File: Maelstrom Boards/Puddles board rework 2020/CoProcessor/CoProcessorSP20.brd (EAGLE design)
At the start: 101.6 x 101.6 mm, 77 parts, among them J1 USB_MINI-B_SMT, P1 RB1-125BAG1A, Q1 310mA/60V/1.6Ω, Q2 310mA/60V/1.6Ω, Q3 310mA/60V/1.6Ω, Q4 310mA/60V/1.6Ω, Q5 310mA/60V/1.6Ω, Q6 310mA/60V/1.6Ω, Q7 310mA/60V/1.6Ω, Q8 310mA/60V/1.6Ω, U1 W5500, U2 STM32F405RGT6, Y1 12MHz, Y2 25MHz, Y3 32.768kHz

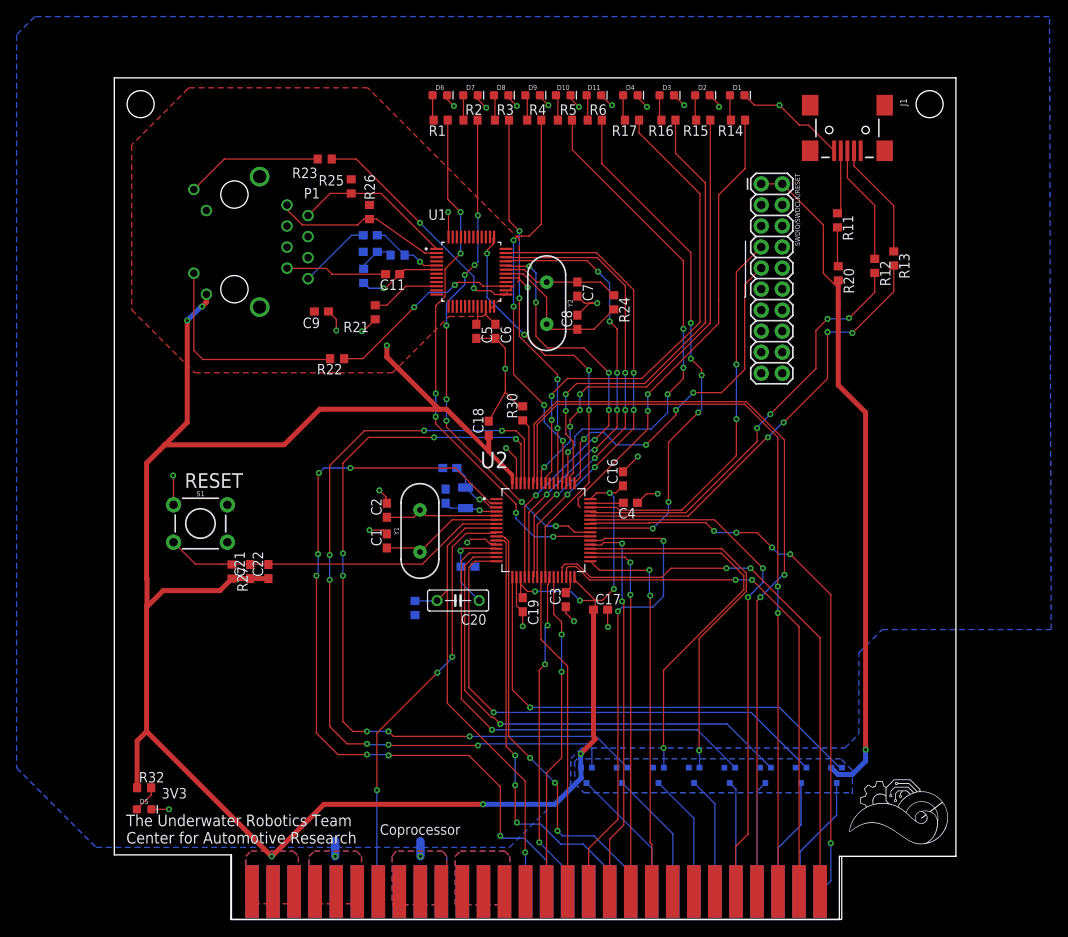
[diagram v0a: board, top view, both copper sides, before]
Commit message: updated puddles board rework ESC and Copro finished
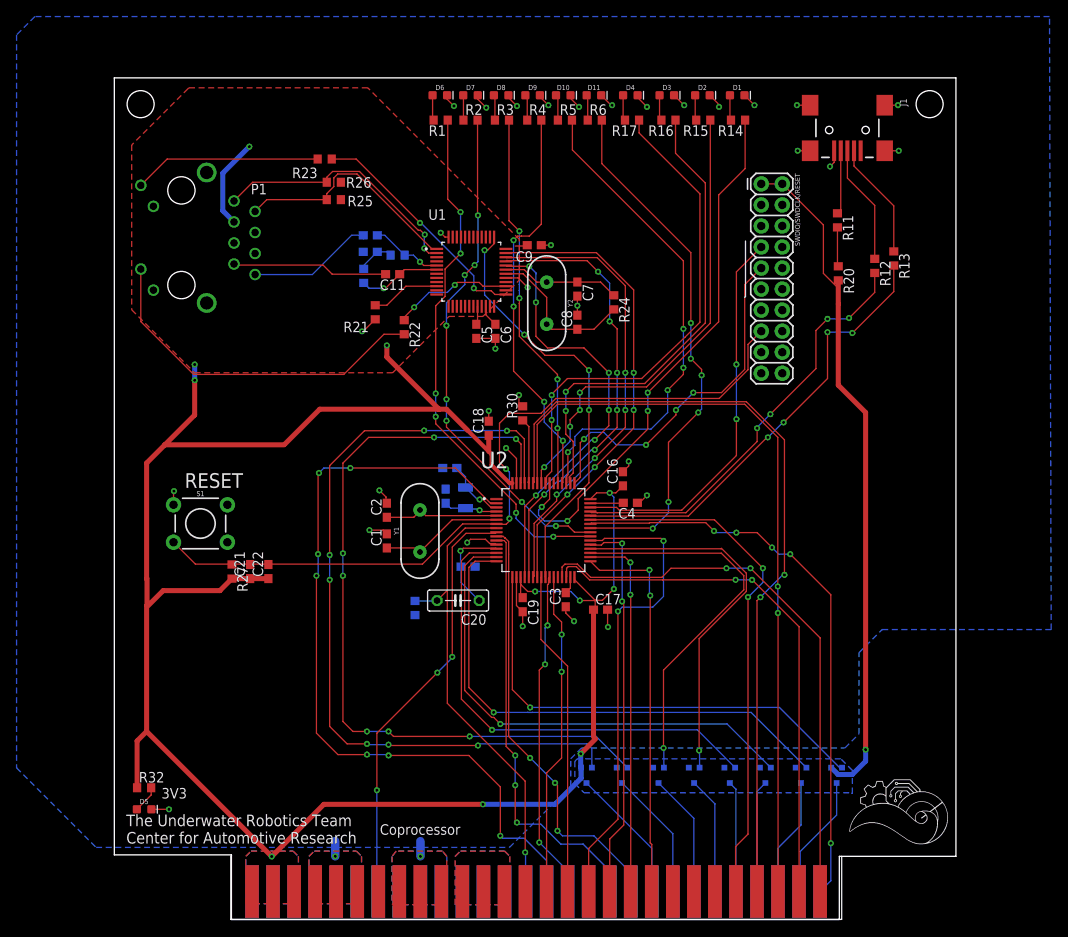
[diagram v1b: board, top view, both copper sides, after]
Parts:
- R1: value 5 -> 65
- R4, R5: value 65 -> 5
- moved C9 26.9 mm to (50.7, 81.4)
- moved R22 8.95 mm to (35.0, 71.5), turned to 270 degrees
- moved P1 6.42 mm to (8.10, 82.3)
- moved R26 5.61 mm to (26.5, 89.0), turned to 0 degrees
- moved R25 2.64 mm to (26.5, 86.9), turned to 0 degrees
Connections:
- removed net N$34: C21.2, C22.2, R27.1, S1.3, U2.7
- new net RESET: C21.2, C22.2, R27.1, S1.3, SWDIO/SWDCLK/RESET.15, U2.7
- net GND: now also J1.S1, J1.S2, J1.S3, J1.S4
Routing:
- net RESET: track 0.00 -> 94.6 mm, vias 0 -> 2
- net N$34: track 42.2 -> 0.00 mm
- net GND: track 103.0 -> 78.8 mm, vias 29 -> 36
- net N$20: track 26.3 -> 42.8 mm
- net N$17: track 21.0 -> 31.6 mm, vias 0 -> 2
- net LED_RED: track 55.2 -> 65.5 mm, vias 2 -> 4
- net N$16: track 19.4 -> 28.6 mm
- net N$22: track 23.5 -> 14.6 mm
- net N$27: track 12.2 -> 18.8 mm
- net N$21: track 16.5 -> 22.7 mm
- net N$26: track 9.28 -> 15.5 mm
- net +3V3: track 357.6 -> 361.0 mm, vias 12 -> 13

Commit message: final commit for ESC board, resistor values changed across boards for order ease
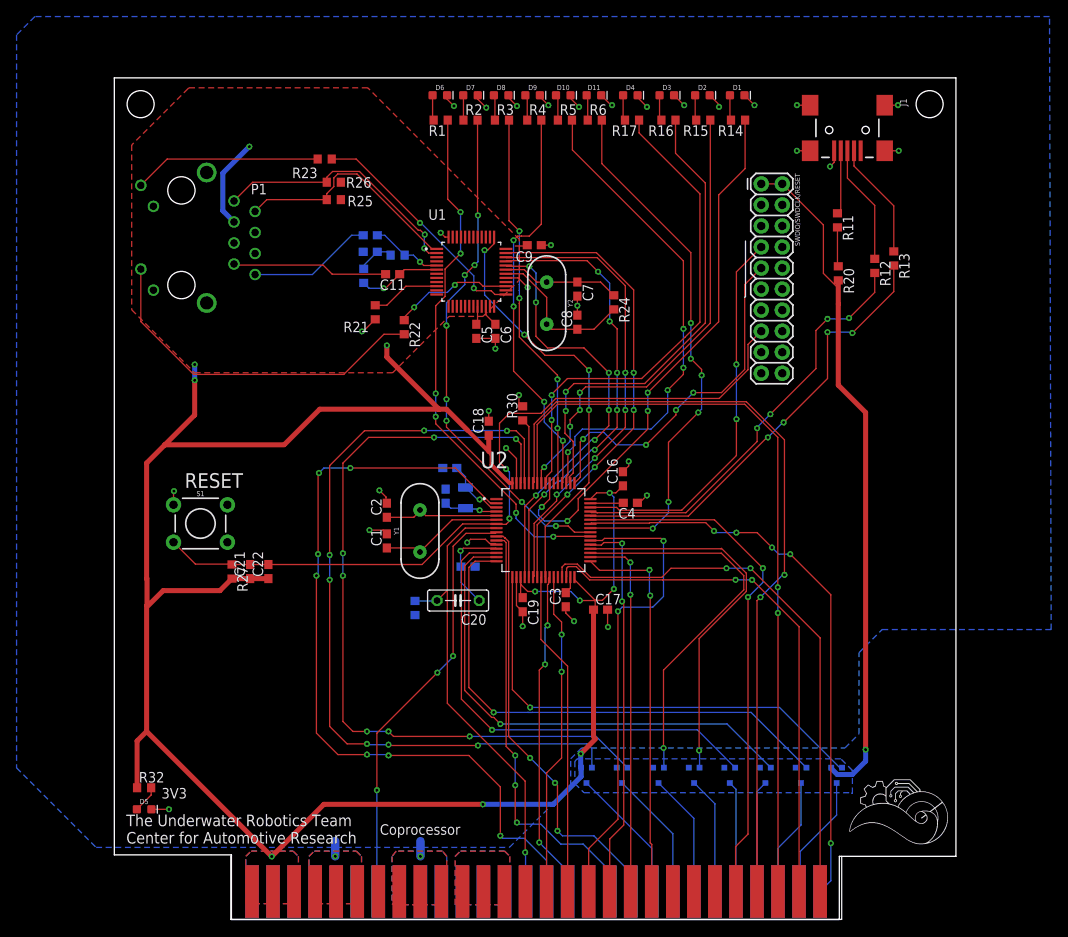
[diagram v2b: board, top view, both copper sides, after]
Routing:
- net PWM_CH1: track 19.2 -> 16.4 mm
- net 5V_CNTRL: track 97.5 -> 96.3 mm
- net MOBO_CNTRL: track 53.0 -> 52.5 mm

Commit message: Changing puddles values
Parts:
- C1, C2, C7, C8: value 18pF -> 30pF
- C13, C14: value 12.5pF -> 18pF
- R1, R14, R15, R2, R3, R6: value 65 -> 68
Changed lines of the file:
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@@
 <?xml version="1.0" encoding="utf-8"?>
 <!DOCTYPE eagle SYSTEM "eagle.dtd">
-<eagle version="9.5.2">
+<eagle version="9.6.2">
 <drawing>
 <settings>
@@
 <attribute name="VALUE" x="62.3" y="98.865" size="0.6096" layer="27" font="vector" ratio="20" align="top-center"/>
 </element>
-<element name="R14" library="rcl" library_urn="urn:adsk.eagle:library:334" package="R0603" package3d_urn="urn:adsk.eagle:package:23555/2" value="65" x="75.3" y="96.5" smashed="yes" rot="R180">
+<element name="R14" library="rcl" library_urn="urn:adsk.eagle:library:334" package="R0603" package3d_urn="urn:adsk.eagle:package:23555/2" value="68" x="75.3" y="96.5" smashed="yes" rot="R180">
 <attribute name="NAME" x="75.935" y="95.865" size="1.27" layer="25" rot="R180"/>
 <attribute name="SPICEPREFIX" value="R" x="94.9" y="154.3" size="1.778" layer="27" rot="R180" display="off"/>
 <attribute name="VALUE" x="75.935" y="98.405" size="1.27" layer="27" rot="R180"/>
 </element>
-<element name="R15" library="rcl" library_urn="urn:adsk.eagle:library:334" package="R0603" package3d_urn="urn:adsk.eagle:package:23555/2" value="65" x="71.1" y="96.5" smashed="yes" rot="R180">
+<element name="R15" library="rcl" library_urn="urn:adsk.eagle:library:334" package="R0603" package3d_urn="urn:adsk.eagle:package:23555/2" value="68" x="71.1" y="96.5" smashed="yes" rot="R180">
 <attribute name="NAME" x="71.735" y="95.865" size="1.27" layer="25" rot="R180"/>
 <attribute name="SPICEPREFIX" value="R" x="95.4" y="157.8" size="1.778" layer="27" rot="R180" display="off"/>
@@
 <attribute name="VALUE" x="39.44" y="46.9" size="0.6096" layer="27" font="vector" ratio="20" rot="R90" align="top-center"/>
 </element>
-<element name="C1" library="rcl" library_urn="urn:adsk.eagle:library:334" package="C0603" package3d_urn="urn:adsk.eagle:package:23616/2" value="18pF" x="32.9" y="45.7" smashed="yes" rot="R90">
+<element name="C1" library="rcl" library_urn="urn:adsk.eagle:library:334" package="C0603" package3d_urn="urn:adsk.eagle:package:23616/2" value="30pF" x="32.9" y="45.7" smashed="yes" rot="R90">
 <attribute name="NAME" x="32.265" y="45.065" size="1.27" layer="25" rot="R90"/>
 <attribute name="SPICEPREFIX" value="C" x="121.4" y="7.3" size="1.778" layer="27" rot="R90" display="off"/>
 <attribute name="VALUE" x="34.805" y="45.065" size="1.27" layer="27" rot="R90"/>
 </element>
-<element name="C2" library="rcl" library_urn="urn:adsk.eagle:library:334" package="C0603" package3d_urn="urn:adsk.eagle:package:23616/2" value="18pF" x="32.9" y="49.4" smashed="yes" rot="R90">
+<element name="C2" library="rcl" library_urn="urn:adsk.eagle:library:334" package="C0603" package3d_urn="urn:adsk.eagle:package:23616/2" value="30pF" x="32.9" y="49.4" smashed="yes" rot="R90">
 <attribute name="NAME" x="32.265" y="48.765" size="1.27" layer="25" rot="R90"/>
 <attribute name="SPICEPREFIX" value="C" x="124.9" y="7.3" size="1.778" layer="27" rot="R90" display="off"/>
@@
 <attribute name="VALUE" x="49.66" y="74.4" size="0.6096" layer="27" font="vector" ratio="20" rot="R270" align="top-center"/>
 </element>
-<element name="C7" library="rcl" library_urn="urn:adsk.eagle:library:334" package="C0603" package3d_urn="urn:adsk.eagle:package:23616/2" value="18pF" x="55.9" y="76.1" smashed="yes" rot="R270">
+<element name="C7" library="rcl" library_urn="urn:adsk.eagle:library:334" package="C0603" package3d_urn="urn:adsk.eagle:package:23616/2" value="30pF" x="55.9" y="76.1" smashed="yes" rot="R270">
 <attribute name="NAME" x="56.535" y="76.735" size="1.27" layer="25" rot="R270"/>
 <attribute name="SPICEPREFIX" value="C" x="54.7" y="125.1" size="1.778" layer="27" rot="R270" display="off"/>
 <attribute name="VALUE" x="53.995" y="76.735" size="1.27" layer="27" rot="R270"/>
 </element>
-<element name="C8" library="rcl" library_urn="urn:adsk.eagle:library:334" package="C0603" package3d_urn="urn:adsk.eagle:package:23616/2" value="18pF" x="55.9" y="72.1" smashed="yes" rot="R90">
+<element name="C8" library="rcl" library_urn="urn:adsk.eagle:library:334" package="C0603" package3d_urn="urn:adsk.eagle:package:23616/2" value="30pF" x="55.9" y="72.1" smashed="yes" rot="R90">
 <attribute name="NAME" x="55.265" y="71.465" size="1.27" layer="25" rot="R90"/>
 <attribute name="SPICEPREFIX" value="C" x="60.6" y="19.4" size="1.778" layer="27" rot="R90" display="off"/>
@@
 <attribute name="VALUE" x="41.357" y="50.9" size="0.6096" layer="28" font="vector" ratio="20" rot="MR90" align="top-center"/>
 </element>
-<element name="C13" library="rcl" library_urn="urn:adsk.eagle:library:334" package="C0603" package3d_urn="urn:adsk.eagle:package:23616/2" value="12.5pF" x="40" y="51.1" smashed="yes" rot="MR90">
+<element name="C13" library="rcl" library_urn="urn:adsk.eagle:library:334" package="C0603" package3d_urn="urn:adsk.eagle:package:23616/2" value="18pF" x="40" y="51.1" smashed="yes" rot="MR90">
 <attribute name="NAME" x="40.635" y="50.465" size="1.27" layer="26" rot="MR90"/>
 <attribute name="SPICEPREFIX" value="C" x="40" y="51.1" size="1.778" layer="28" rot="MR90" display="off"/>
 <attribute name="VALUE" x="38.095" y="50.465" size="1.27" layer="28" rot="MR90"/>
 </element>
-<element name="C14" library="rcl" library_urn="urn:adsk.eagle:library:334" package="C0603" package3d_urn="urn:adsk.eagle:package:23616/2" value="12.5pF" x="40.5" y="54.5" smashed="yes" rot="MR0">
+<element name="C14" library="rcl" library_urn="urn:adsk.eagle:library:334" package="C0603" package3d_urn="urn:adsk.eagle:package:23616/2" value="18pF" x="40.5" y="54.5" smashed="yes" rot="MR0">
 <attribute name="NAME" x="41.135" y="55.135" size="1.27" layer="26" rot="MR0"/>
 <attribute name="SPICEPREFIX" value="C" x="40.5" y="54.5" size="1.778" layer="28" rot="MR0" display="off"/>
@@
 <attribute name="VALUE" x="39.3" y="98.865" size="0.6096" layer="27" font="vector" ratio="20" align="top-center"/>
 </element>
-<element name="R1" library="rcl" library_urn="urn:adsk.eagle:library:334" package="R0603" package3d_urn="urn:adsk.eagle:package:23555/2" value="65" x="39.4" y="96.5" smashed="yes" rot="R180">
+<element name="R1" library="rcl" library_urn="urn:adsk.eagle:library:334" package="R0603" package3d_urn="urn:adsk.eagle:package:23555/2" value="68" x="39.4" y="96.5" smashed="yes" rot="R180">
 <attribute name="NAME" x="40.035" y="95.865" size="1.27" layer="25" rot="R180"/>
 <attribute name="SPICEPREFIX" value="R" x="39.4" y="99.1" size="1.778" layer="27" rot="R180" display="off"/>
@@
 <attribute name="VALUE" x="57.9" y="98.865" size="0.6096" layer="27" font="vector" ratio="20" align="top-center"/>
 </element>
-<element name="R2" library="rcl" library_urn="urn:adsk.eagle:library:334" package="R0603" package3d_urn="urn:adsk.eagle:package:23555/2" value="65" x="43" y="96.5" smashed="yes">
+<element name="R2" library="rcl" library_urn="urn:adsk.eagle:library:334" package="R0603" package3d_urn="urn:adsk.eagle:package:23555/2" value="68" x="43" y="96.5" smashed="yes">
 <attribute name="NAME" x="42.365" y="97.135" size="1.27" layer="25"/>
 <attribute name="SPICEPREFIX" value="R" x="43" y="96.5" size="1.778" layer="27" display="off"/>
 <attribute name="VALUE" x="42.365" y="94.595" size="1.27" layer="27"/>
 </element>
-<element name="R3" library="rcl" library_urn="urn:adsk.eagle:library:334" package="R0603" package3d_urn="urn:adsk.eagle:package:23555/2" value="65" x="46.8" y="96.5" smashed="yes">
+<element name="R3" library="rcl" library_urn="urn:adsk.eagle:library:334" package="R0603" package3d_urn="urn:adsk.eagle:package:23555/2" value="68" x="46.8" y="96.5" smashed="yes">
 <attribute name="NAME" x="46.165" y="97.135" size="1.27" layer="25"/>
 <attribute name="SPICEPREFIX" value="R" x="46.8" y="96.5" size="1.778" layer="27" display="off"/>
@@
 <attribute name="VALUE" x="53.765" y="94.595" size="1.27" layer="27"/>
 </element>
-<element name="R6" library="rcl" library_urn="urn:adsk.eagle:library:334" package="R0603" package3d_urn="urn:adsk.eagle:package:23555/2" value="65" x="58" y="96.5" smashed="yes">
+<element name="R6" library="rcl" library_urn="urn:adsk.eagle:library:334" package="R0603" package3d_urn="urn:adsk.eagle:package:23555/2" value="68" x="58" y="96.5" smashed="yes">
 <attribute name="NAME" x="57.365" y="97.135" size="1.27" layer="25"/>
 <attribute name="SPICEPREFIX" value="R" x="58" y="96.5" size="1.778" layer="27" display="off"/>
